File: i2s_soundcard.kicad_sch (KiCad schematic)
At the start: 29 parts, among them J1 Conn_01x08, J2 Conn_01x06, J3 Conn_02x20_Odd_Even, J5 Conn_01x03, U1 TLV320AIC3206IRSBR, U4 FSA2275UMX, U6 TLV7111830DSER, U7 TPD4E02B04DQAR, U8 TPD4E02B04DQAR

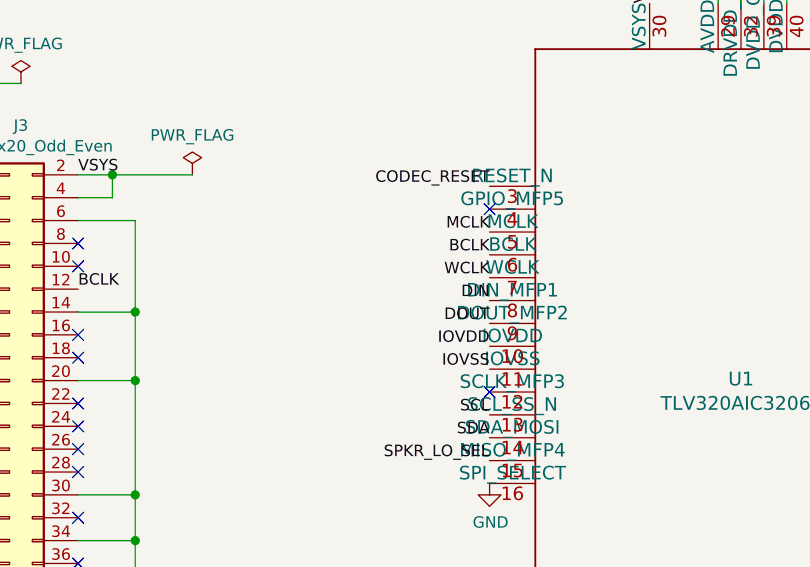
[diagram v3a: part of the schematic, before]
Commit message: Add 27R resistors to transmit side of i2s lines as recommended by aic3206 datasheet.
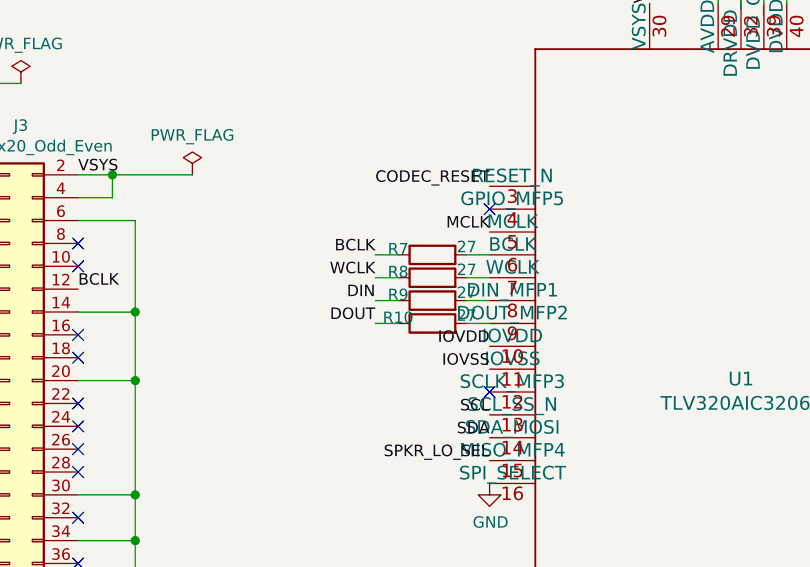
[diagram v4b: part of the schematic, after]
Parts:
- added R10, R7, R8, R9: 27, Resistor_SMD:R_0402_1005Metric, symbol Device:R
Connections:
- net BCLK: now also R7.1; no longer U1.6 (BCLK)
- net DIN: now also R9.1; no longer U1.8 (DIN_MFP1)
- net DOUT: now also R10.1; no longer U1.9 (DOUT_MFP2)
- net WCLK: now also R8.1; no longer U1.7 (WCLK)
- new net: R7.2, U1.6 (BCLK)
- new net: R8.2, U1.7 (WCLK)
- new net: R10.2, U1.9 (DOUT_MFP2)
- new net: R9.2, U1.8 (DIN_MFP1)
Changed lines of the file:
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@@
+    (stroke (width 0) (type solid) (color 0 0 0 0))
+  )
+  (wire (pts (xy 95.25 165.1) (xy 97.79 165.1))
+    (stroke (width 0) (type solid) (color 0 0 0 0))
+  )
+  (wire (pts (xy 95.25 167.64) (xy 97.79 167.64))
+    (stroke (width 0) (type solid) (color 0 0 0 0))
+  )
+  (wire (pts (xy 95.25 170.18) (xy 97.79 170.18))
+    (stroke (width 0) (type solid) (color 0 0 0 0))
+  )
+  (wire (pts (xy 95.25 172.72) (xy 97.79 172.72))
+    (stroke (width 0) (type solid) (color 0 0 0 0))
+  )
+  (wire (pts (xy 105.41 165.1) (xy 107.95 165.1))
+    (stroke (width 0) (type solid) (color 0 0 0 0))
+  )
+  (wire (pts (xy 105.41 167.64) (xy 107.95 167.64))
+    (stroke (width 0) (type solid) (color 0 0 0 0))
+  )
+  (wire (pts (xy 105.41 170.18) (xy 107.95 170.18))
+    (stroke (width 0) (type solid) (color 0 0 0 0))
+  )
+  (wire (pts (xy 105.41 172.72) (xy 107.95 172.72))
     (stroke (width 0) (type solid) (color 0 0 0 0))
   )
@@
     (effects (font (size 1.27 1.27)) (justify left bottom))
   )
+  (label "BCLK" (at 95.25 165.1 180)
+    (effects (font (size 1.27 1.27)) (justify right bottom))
+  )
+  (label "WCLK" (at 95.25 167.64 180)
+    (effects (font (size 1.27 1.27)) (justify right bottom))
+  )
+  (label "DIN" (at 95.25 170.18 180)
+    (effects (font (size 1.27 1.27)) (justify right bottom))
+  )
+  (label "DOUT" (at 95.25 172.72 180)
+    (effects (font (size 1.27 1.27)) (justify right bottom))
+  )
   (label "CODEC_RESET" (at 107.95 157.48 180)
     (effects (font (size 1.27 1.27)) (justify right bottom))
   )
   (label "MCLK" (at 107.95 162.56 180)
-    (effects (font (size 1.27 1.27)) (justify right bottom))
-  )
-  (label "BCLK" (at 107.95 165.1 180)
-    (effects (font (size 1.27 1.27)) (justify right bottom))
-  )
-  (label "WCLK" (at 107.95 167.64 180)
-    (effects (font (size 1.27 1.27)) (justify right bottom))
-  )
-  (label "DIN" (at 107.95 170.18 180)
-    (effects (font (size 1.27 1.27)) (justify right bottom))
-  )
-  (label "DOUT" (at 107.95 172.72 180)
     (effects (font (size 1.27 1.27)) (justify right bottom))
   )
@@
     )
     (property "Datasheet" "~" (id 3) (at 92.71 96.52 0)
+      (effects (font (size 1.27 1.27)) hide)
+    )
+    (pin "1")
+    (pin "2")
+  )
+  (symbol (lib_id "Device:R") (at 101.6 165.1 90) (unit 1)
+    (in_bom yes) (on_board yes)
+    (property "Reference" "R7" (id 0) (at 97.79 164.4608 90))
+    (property "Value" "27" (id 1) (at 105.41 164.2195 90))
+    (property "Footprint" "Resistor_SMD:R_0402_1005Metric" (id 2) (at 101.6 166.878 90)
+      (effects (font (size 1.27 1.27)) hide)
+    )
+    (property "Datasheet" "~" (id 3) (at 101.6 165.1 0)
+      (effects (font (size 1.27 1.27)) hide)
+    )
+    (pin "1")
+    (pin "2")
+  )
+  (symbol (lib_id "Device:R") (at 101.6 167.64 90) (unit 1)
+    (in_bom yes) (on_board yes)
+    (property "Reference" "R8" (id 0) (at 97.79 167.0008 90))
+    (property "Value" "27" (id 1) (at 105.41 166.7595 90))
+    (property "Footprint" "Resistor_SMD:R_0402_1005Metric" (id 2) (at 101.6 169.418 90)
+      (effects (font (size 1.27 1.27)) hide)
+    )
+    (property "Datasheet" "~" (id 3) (at 101.6 167.64 0)
+      (effects (font (size 1.27 1.27)) hide)
+    )
+    (pin "1")
+    (pin "2")
+  )
+  (symbol (lib_id "Device:R") (at 101.6 170.18 90) (unit 1)
+    (in_bom yes) (on_board yes)
+    (property "Reference" "R9" (id 0) (at 97.79 169.5408 90))
+    (property "Value" "27" (id 1) (at 105.41 169.2995 90))
+    (property "Footprint" "Resistor_SMD:R_0402_1005Metric" (id 2) (at 101.6 171.958 90)
+      (effects (font (size 1.27 1.27)) hide)
+    )
+    (property "Datasheet" "~" (id 3) (at 101.6 170.18 0)
+      (effects (font (size 1.27 1.27)) hide)
+    )
+    (pin "1")
+    (pin "2")
+  )
+  (symbol (lib_id "Device:R") (at 101.6 172.72 90) (unit 1)
+    (in_bom yes) (on_board yes)
+    (property "Reference" "R10" (id 0) (at 97.79 172.0808 90))
+    (property "Value" "27" (id 1) (at 105.41 171.8395 90))
+    (property "Footprint" "Resistor_SMD:R_0402_1005Metric" (id 2) (at 101.6 174.498 90)
+      (effects (font (size 1.27 1.27)) hide)
+    )
+    (property "Datasheet" "~" (id 3) (at 101.6 172.72 0)
       (effects (font (size 1.27 1.27)) hide)
     )
@@
       (reference "R6") (unit 1) (value "R") (footprint "Resistor_SMD:R_0402_1005Metric")
     )
+    (path "/0ca0db7d-9a9e-456a-975b-c25873228a03"
+      (reference "R7") (unit 1) (value "27") (footprint "Resistor_SMD:R_0402_1005Metric")
+    )
+    (path "/221c4def-0960-4135-a790-b65e6e28ecc2"
+      (reference "R8") (unit 1) (value "27") (footprint "Resistor_SMD:R_0402_1005Metric")
+    )
+    (path "/c8d5b61f-2ba7-4ce1-bf87-4946504ff45c"
+      (reference "R9") (unit 1) (value "27") (footprint "Resistor_SMD:R_0402_1005Metric")
+    )
+    (path "/8fefca81-bcbd-4018-863f-6f30deaa0b26"
+      (reference "R10") (unit 1) (value "27") (footprint "Resistor_SMD:R_0402_1005Metric")
+    )
     (path "/c71bb412-9e6e-4630-9b86-aa272a0438c1"

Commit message: Refactor everything but headers into a hierarchical sheet.
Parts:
- removed C1, C11: 100nF, Capacitor_SMD:C_0402_1005Metric, symbol Device:C
- removed C10, C13, C14, C23, C24, C4: 10uF, Capacitor_SMD:C_0402_1005Metric, symbol Device:C
- removed C12, C9: 0.1u, Capacitor_SMD:C_0402_1005Metric, symbol Device:C
- removed C15, C22, C8: 0.1uF, Capacitor_SMD:C_0402_1005Metric, symbol Device:C
- removed C2: 1uF, Capacitor_SMD:C_0402_1005Metric, symbol Device:C
- removed C3, C5: 2.2uF, Capacitor_SMD:C_0402_1005Metric, symbol Device:C
- removed J1: Conn_01x08, footprints:FF18-8A-R11AD-B-3H, symbol Connector_Generic:Conn_01x08
- removed J2: Conn_01x06, footprints:78171-0004, symbol Connector_Generic:Conn_01x06
- removed R1: 2.7k, Resistor_SMD:R_0402_1005Metric, symbol Device:R
- removed R10, R7, R8, R9: 27, Resistor_SMD:R_0402_1005Metric, symbol Device:R
- removed R2, R3: 1k, Resistor_SMD:R_0402_1005Metric, symbol Device:R
- removed R6: R, Resistor_SMD:R_0402_1005Metric, symbol Device:R
- removed U1: TLV320AIC3206IRSBR, footprints:TLV320AIC3206IRSBR, symbol TLV320AIC3206IRSBR:TLV320AIC3206IRSBR
- removed U4: FSA2275UMX, footprints:FSA2275, symbol FSA2275UMX:FSA2275UMX
- removed U6: TLV7111830DSER, footprints:TLV7111830DSER, symbol TLV7111830DSER:TLV7111830DSER
- removed U7, U8: TPD4E02B04DQAR, footprints:TPD4E02B04DQAR, symbol TPD4E02B04DQAR:TPD4E02B04DQAR
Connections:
- no-connect marks 26 -> 19
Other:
- sheet spkr_amp_left renamed codec and amp
- removed sheet spkr_amp_right
- sheet codec and amp: file spkr_amp.kicad_sch -> codec_and_amp.kicad_sch
- sheet codec and amp ports: added BCLK, DIN, DOUT, IOVDD, LDO_EN1, LOL, LOR, SCL, SDA, VSYS, WCLK, ~AMP_SHUTDOWN, ~CODEC_RESET; removed LINEIN, SPKR+, SPKR-, VDD, ~SHUTDOWN
- moved on the sheet: J5
